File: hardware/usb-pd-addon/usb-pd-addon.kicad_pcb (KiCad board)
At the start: 4 copper layers, 48 x 40 mm, 61 parts, among them J1 Conn_02x10_Odd_Even, J10 Conn_01x03_Male, J11 Conn_01x03_Male, J12 Conn_01x03_Male, J2 Conn_02x10_Odd_Even, J3 USB_TYPE_C, J4 USB_TYPE_C, J5 Conn_01x03_Male, J6 TPAS, J7 TPBS, J8 Conn_02x03_Odd_Even, U1 FUSB302B, U2 AP2171W, U3 SN74AVC1T45DBVR, U4 SN74AVC1T45DBVR, U5 SN74AVC1T45DBVR, U6 SN74AVC1T45DBVR, U7 AP2127K-ADJ

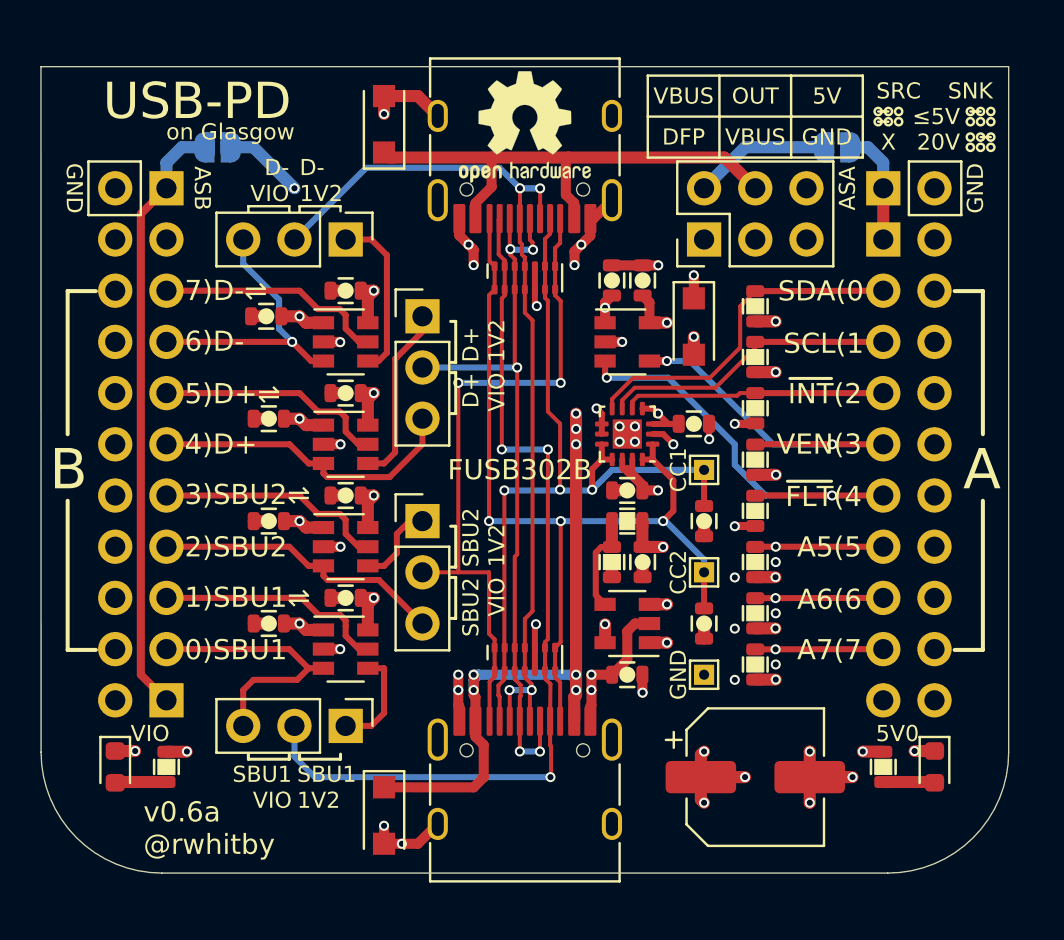
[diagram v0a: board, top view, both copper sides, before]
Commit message: v0.7a: analog switches instead of jumpers
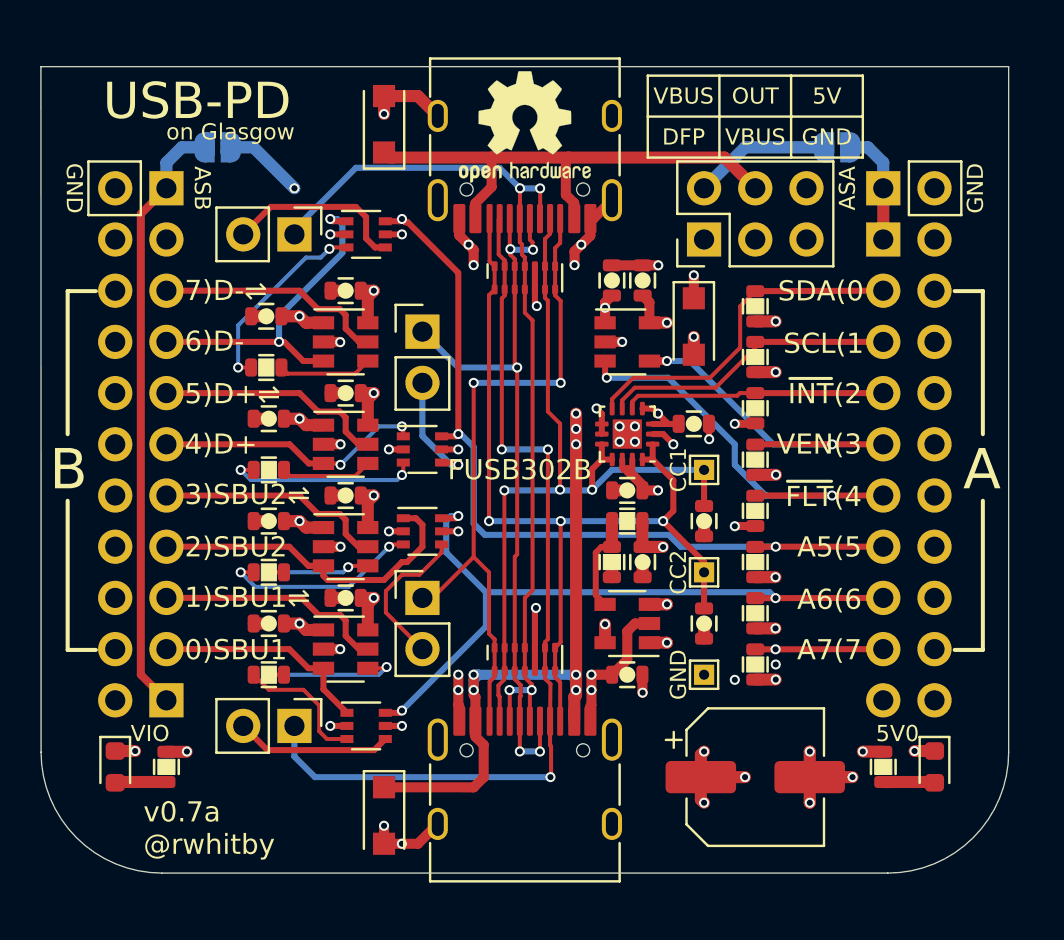
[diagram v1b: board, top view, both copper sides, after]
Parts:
- removed J12: Conn_01x03_Male, Connector_PinHeader_2.54mm:PinHeader_1x03_P2.54mm_Vertical
- added J9: Conn_01x02, Connector_PinHeader_2.54mm:PinHeader_1x02_P2.54mm_Vertical, F.Cu at (50.8, 45.2)
- added R11: 100R, pkl_dipol:R_0603, F.Cu at (43.1, 47.0)
- added R12: 100R, pkl_dipol:R_0603, F.Cu at (43.2, 57.1)
- added R13: 100R, pkl_dipol:R_0603, F.Cu at (43.2, 52.1)
- added R14: 100R, pkl_dipol:R_0603, F.Cu at (43.2, 62.2)
- added U10: NC7SB3157P6X, Package_TO_SOT_SMD:SOT-363_SC-70-6, F.Cu at (50.8, 55.1)
- added U11: NC7SB3157P6X, Package_TO_SOT_SMD:SOT-363_SC-70-6, F.Cu at (48.0, 64.8)
- added U8: NC7SB3157P6X, Package_TO_SOT_SMD:SOT-363_SC-70-6, F.Cu at (48.0, 40.4)
- added U9: NC7SB3157P6X, Package_TO_SOT_SMD:SOT-363_SC-70-6, F.Cu at (50.8, 51.1)
- J10, J11, J5: value Conn_01x03_Male -> Conn_01x02; footprint Connector_PinHeader_2.54mm:PinHeader_1x03_P2.54mm_Vertical -> Connector_PinHeader_2.54mm:PinHeader_1x02_P2.54mm_Vertical
- R6, R7: value 2K2 -> 1K
- moved J11 21.3 mm to (44.5, 64.8), turned to 270 degrees
- moved J10 3.81 mm to (50.8, 58.4)
- moved J5 2.55 mm to (44.5, 40.4)
- renumbered R11 to R10, R13 to R15, R33 to R16
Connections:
- net /A5 renamed /~USB_1V2
- net /A6 renamed /~SBU_1V2
- J10 pad 1: /SBU2_1V2 -> /SBU2
- J10 pad 2: /SBU2 -> Net-(J10-Pad2)
- J11 pad 1: /USBP_1V2 -> /SBU1
- J11 pad 2: /USBP -> Net-(J11-Pad2)
- J5 pad 1: /USBN_1V2 -> /USBN
- J5 pad 2: /USBN -> Net-(J5-Pad2)
- R6 pad 1: Net-(R6-Pad1) -> GND
- R7 pad 1: Net-(R7-Pad1) -> GND
- U3 pad 4: /USBN_1V2 -> Net-(R11-Pad1)
- U4 pad 4: /SBU2_1V2 -> Net-(R12-Pad1)
- U5 pad 4: /USBP_1V2 -> Net-(R13-Pad1)
- U6 pad 4: /SBU1_1V2 -> Net-(R14-Pad1)
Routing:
- net +5V: track 114.4 -> 162.9 mm, vias 14 -> 16
- net /~USB_1V2: track 6.35 -> 40.3 mm, vias 1 -> 3
- net /~SBU_1V2: track 6.35 -> 35.2 mm, vias 1 -> 3
- net Net-(R12-Pad2): track 0.00 -> 9.88 mm, vias 0 -> 2
- net Net-(R11-Pad2): track 0.00 -> 9.73 mm, vias 0 -> 2
- net Net-(R13-Pad2): track 0.00 -> 9.61 mm, vias 0 -> 2
- net Net-(J5-Pad2): track 0.00 -> 9.06 mm
- net /USBP_1V2: track 8.89 -> 0.00 mm
- net /USBN_1V2: track 8.33 -> 0.00 mm
- net Net-(J11-Pad2): track 0.00 -> 7.77 mm
- net Net-(J10-Pad2): track 0.00 -> 7.59 mm
- net Net-(R14-Pad1): track 0.00 -> 7.45 mm, vias 0 -> 2
- net Net-(R14-Pad2): track 0.00 -> 6.69 mm
- net GND: track 201.6 -> 207.5 mm, vias 48 -> 52
- net Net-(J9-Pad2): track 0.00 -> 5.88 mm, vias 0 -> 1
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- removed copper zone on In2.Cu, net +3V3
- removed copper zone on In2.Cu, net +5V
- removed copper zone on In2.Cu, net /1.2V
- removed copper zone on In2.Cu, net /VBUS
- removed copper zone on In2.Cu, net /VBUS_DFP
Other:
- board text added: "v0.7a @rwhitby"
- board text added: "v0.7a CC-BY-SA"
- board text removed: "20V"
- board text removed: "D+ 1V2"
- board text removed: "D+ VIO"
- board text removed: "D- 1V2"
- board text removed: "D- VIO"
- board text removed: "SBU1 1V2"
- board text removed: "SBU1 VIO"
- board text removed: "SBU2 1V2"
- board text removed: "SBU2 VIO"
- board text removed: "SNK"
- board text removed: "SRC"
- board text removed: "X"
- board text removed: "v0.6a @rwhitby"
- board text removed: "v0.6a CC-BY-SA"
- board text removed: "≤5V"

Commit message: Interim version for review
Changed level shifters to smaller footprint.
Added pull-down resistors on direction signals and analog switch selects.
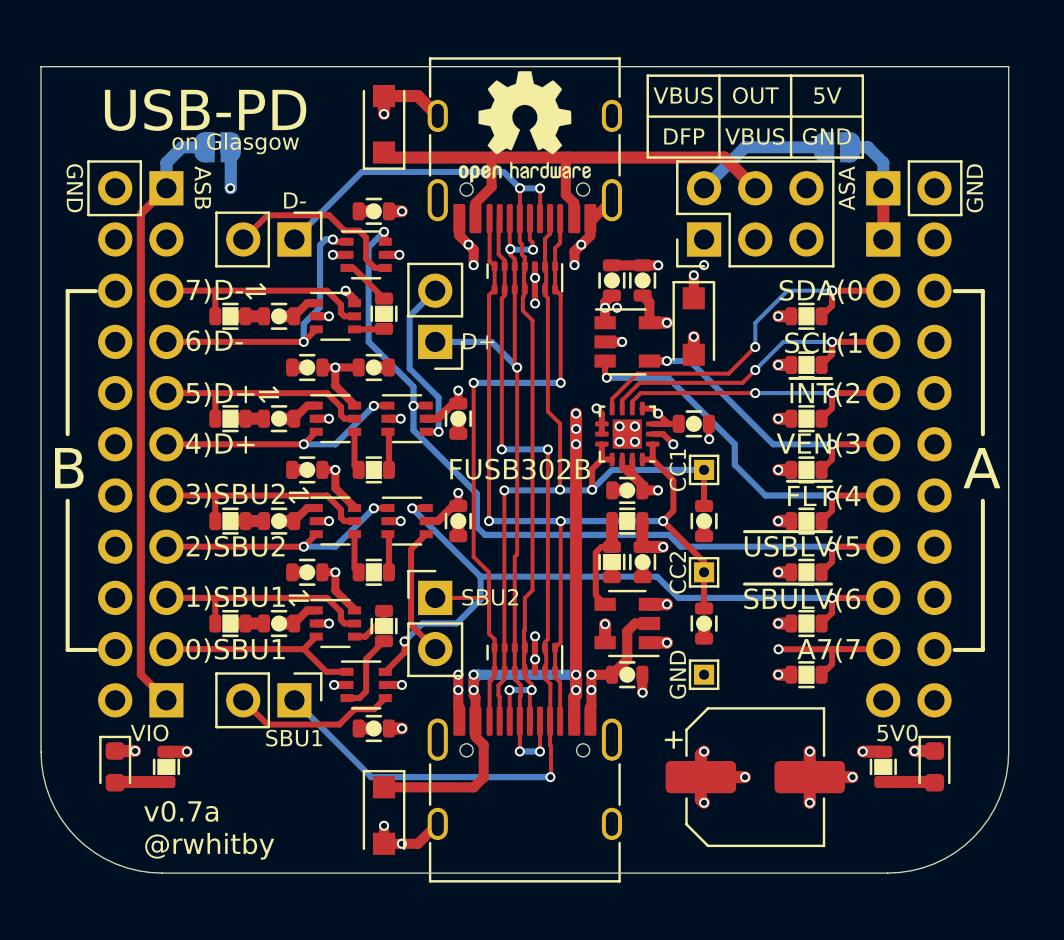
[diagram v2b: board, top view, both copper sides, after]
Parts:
- added C18: 0.1u, pkl_dipol:C_0603, F.Cu at (48.4, 39.2)
- added C19: 0.1u, pkl_dipol:C_0603, F.Cu at (52.6, 49.5)
- added C20: 0.1u, pkl_dipol:C_0603, F.Cu at (52.6, 54.6)
- added C21: 0.1u, pkl_dipol:C_0603, F.Cu at (48.4, 64.9)
- added R17: 100K, pkl_dipol:R_0603, F.Cu at (41.3, 44.5)
- added R18: 100K, pkl_dipol:R_0603, F.Cu at (41.3, 54.6)
- added R19: 100K, pkl_dipol:R_0603, F.Cu at (41.3, 49.5)
- added R20: 100K, pkl_dipol:R_0603, F.Cu at (41.3, 59.7)
- R6, R7: value 1K -> 100K
- U3, U4, U5: value SN74AVC1T45DBVR -> SN74AVC1T45DCKR; footprint Package_TO_SOT_SMD:SOT-23-6 -> Package_TO_SOT_SMD:SOT-363_SC-70-6
- U6: footprint Package_TO_SOT_SMD:SOT-23-6 -> Package_TO_SOT_SMD:SOT-363_SC-70-6
- moved R11 6.42 mm to (48.9, 44.3), turned to 90 degrees
- moved R14 6.20 mm to (48.9, 59.8), turned to 270 degrees
- moved R12 5.21 mm to (48.4, 57.1), turned to 0 degrees
- moved R13 5.21 mm to (48.4, 52.1), turned to 0 degrees
- moved C3 4.06 mm to (48.4, 47.0), turned to 0 degrees
- moved R3 2.59 mm to (69.8, 49.5), turned to 0 degrees
- moved R4 2.59 mm to (69.8, 52.1), turned to 0 degrees
- moved R5 2.59 mm to (69.8, 54.6), turned to 180 degrees
- moved R6 2.59 mm to (69.8, 57.1), turned to 0 degrees
- moved R7 2.59 mm to (69.8, 59.7), turned to 0 degrees
- moved R8 2.59 mm to (69.8, 62.2), turned to 0 degrees
- moved R1 2.59 mm to (69.8, 44.5), turned to 0 degrees
- moved R2 2.57 mm to (69.8, 46.9), turned to 0 degrees
- moved C12 2.29 mm to (45.1, 57.1)
- moved C4 2.29 mm to (45.1, 52.1)
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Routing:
- net +5V: track 162.9 -> 171.5 mm, vias 16 -> 17
- net Net-(R12-Pad2): track 9.88 -> 1.91 mm, vias 2 -> 0
- net Net-(R13-Pad2): track 9.61 -> 1.91 mm, vias 2 -> 0
- net Net-(R11-Pad2): track 9.73 -> 2.47 mm, vias 2 -> 0
- net Net-(R14-Pad1): track 7.45 -> 2.19 mm, vias 2 -> 0
- net /SBU2_3V3: track 16.5 -> 12.7 mm, vias 0 -> 2
- net Net-(R12-Pad1): track 5.54 -> 1.97 mm, vias 2 -> 0
- net Net-(R11-Pad1): track 4.67 -> 1.47 mm
- net Net-(J9-Pad2): track 5.88 -> 8.99 mm
- net /1.2V: track 58.3 -> 61.1 mm
- net Net-(R14-Pad2): track 6.69 -> 3.95 mm
- net Net-(R13-Pad1): track 4.61 -> 1.97 mm
- net /USBN_3V3: track 16.9 -> 14.3 mm
- net /~FLT: track 21.4 -> 19.1 mm
- net /VEN: track 17.1 -> 14.8 mm
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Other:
- board text added: "5)~USBLV"
- board text added: "6)~SBULV"
- board text added: "D+"
- board text added: "D-"
- board text added: "SBU1"
- board text added: "SBU2"
- board text added: "~SBULV~(6"
- board text added: "~USBLV~(5"
- board text removed: "5)A5"
- board text removed: "6)A6"
- board text removed: "A5(5"
- board text removed: "A6(6"

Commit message: Widened some power traces.
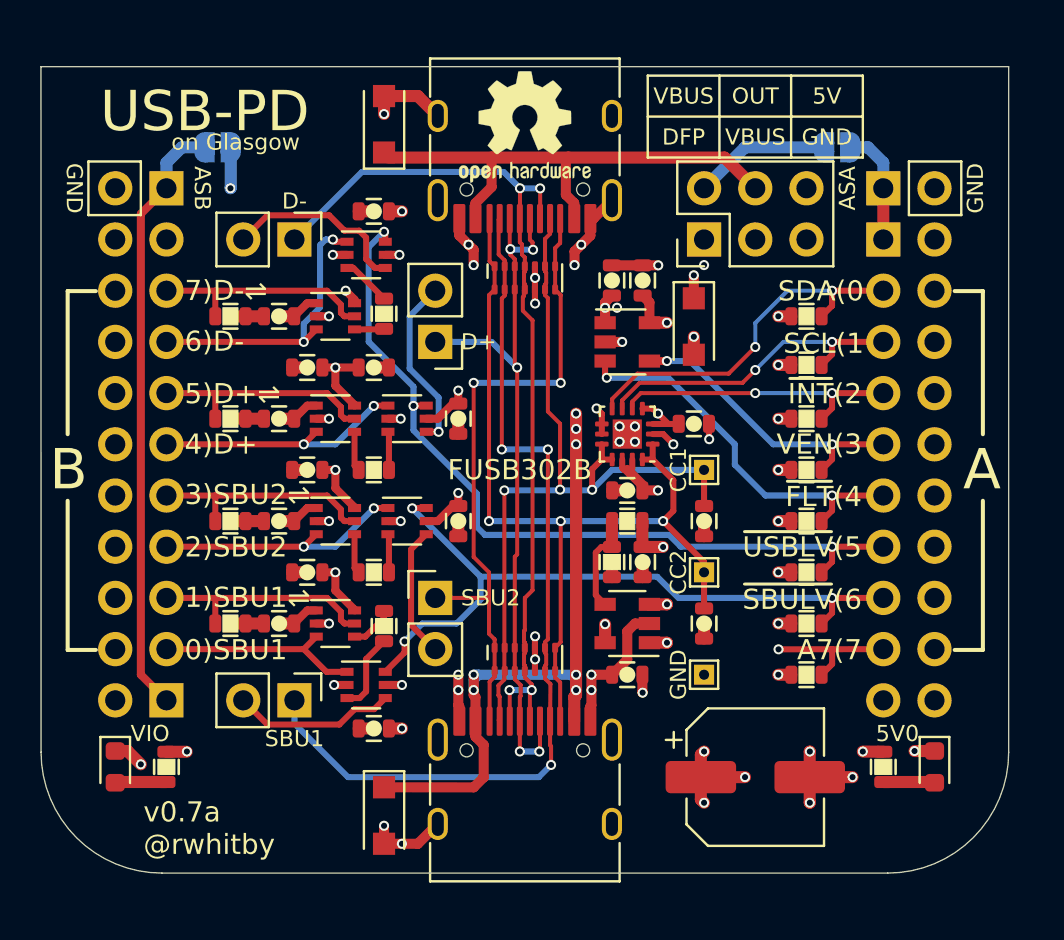
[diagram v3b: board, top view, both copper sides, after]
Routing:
- net +5V: track 171.5 -> 172.5 mm
- net GND: track 209.6 -> 210.2 mm
- net /SDA: vias 3 -> 2

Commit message: v0.8a: Colocated D+/D- and SBU1/SBU2 jumpers. Moved ASA/ASB jumpers away from Glasgow headers.
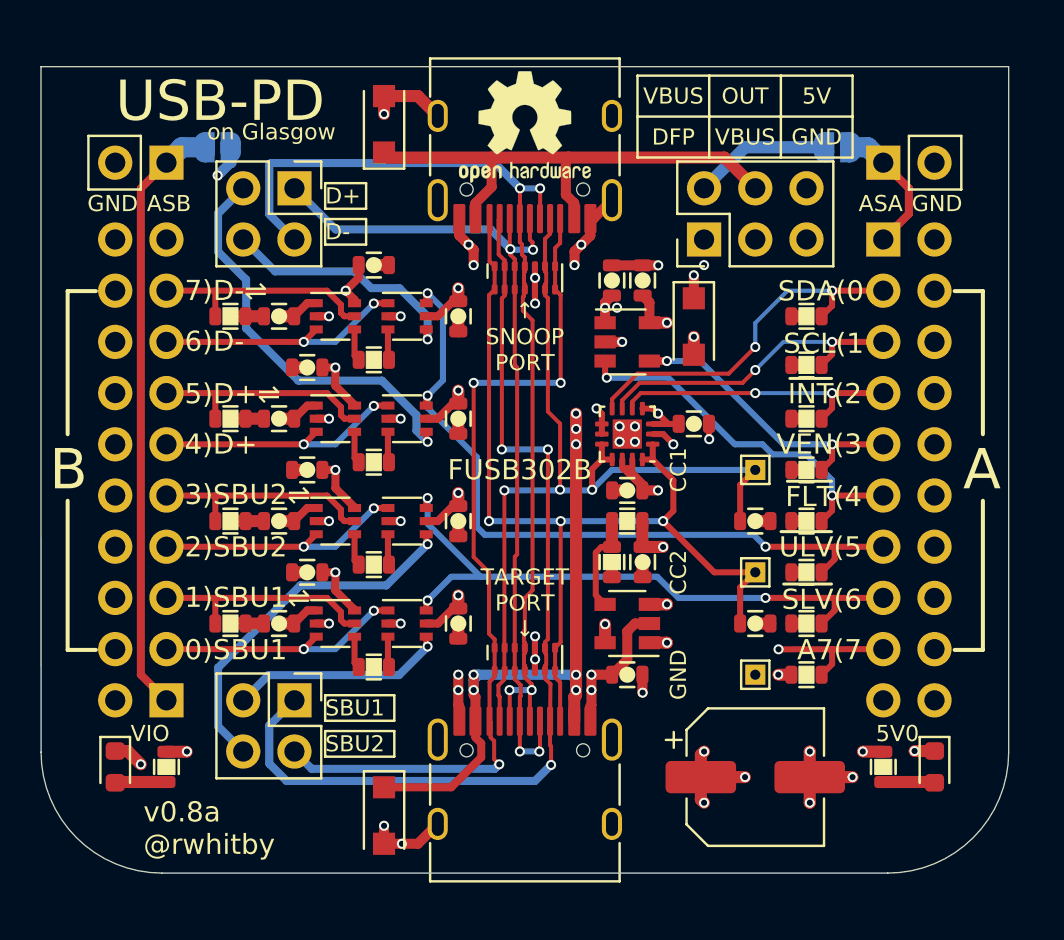
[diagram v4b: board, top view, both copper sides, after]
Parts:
- removed J10, J5: Conn_01x02, Connector_PinHeader_2.54mm:PinHeader_1x02_P2.54mm_Vertical
- J11, J9: value Conn_01x02 -> Conn_02x02; footprint Connector_PinHeader_2.54mm:PinHeader_1x02_P2.54mm_Vertical -> Connector_PinHeader_2.54mm:PinHeader_2x02_P2.54mm_Vertical
- moved J9 10.3 mm to (44.5, 38.1), turned to 270 degrees
- moved C21 6.68 mm to (52.6, 59.7), turned to 270 degrees
- moved C18 6.68 mm to (52.6, 44.5), turned to 270 degrees
- moved C3 5.08 mm to (48.4, 41.9)
- moved U11 3.66 mm to (50.0, 59.7)
- moved U8 3.66 mm to (50.0, 44.5)
- moved C15 2.54 mm to (67.3, 54.6), turned to 180 degrees
- moved C17 2.54 mm to (67.3, 59.7), turned to 180 degrees
- moved TP1 2.54 mm to (67.3, 52.1)
- moved TP2 2.54 mm to (67.3, 57.1)
- moved TP3 2.54 mm to (67.3, 62.2)
- moved R11 2.34 mm to (48.4, 46.6), turned to 0 degrees
- moved R14 2.09 mm to (48.4, 61.8), turned to 0 degrees
- moved J6 1.27 mm to (73.7, 36.8)
- moved J7 1.27 mm to (38.1, 36.8)
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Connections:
- J11 pad 2: Net-(J11-Pad2) -> /SBU2
- J9 pad 2: Net-(J9-Pad2) -> /USBN
- U10 pad 4: Net-(J10-Pad2) -> Net-(J11-Pad4)
- U11 pad 4: Net-(J11-Pad2) -> Net-(J11-Pad3)
- U8 pad 4: Net-(J5-Pad2) -> Net-(J9-Pad4)
- U9 pad 4: Net-(J9-Pad2) -> Net-(J9-Pad3)
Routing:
- net Net-(J9-Pad3): track 0.00 -> 20.3 mm, vias 0 -> 1
- net Net-(J11-Pad4): track 0.00 -> 18.1 mm, vias 0 -> 1
- net Net-(J9-Pad4): track 0.00 -> 12.4 mm, vias 0 -> 1
- net +5V: track 172.5 -> 160.6 mm, vias 17 -> 15
- net Net-(J11-Pad3): track 0.00 -> 10.8 mm, vias 0 -> 1
- net /SBU2: track 32.8 -> 43.1 mm, vias 2 -> 3
- net Net-(J5-Pad2): track 9.25 -> 0.00 mm
- net Net-(J9-Pad2): track 8.99 -> 0.00 mm, vias 1 -> 0
- net Net-(J11-Pad2): track 8.09 -> 0.00 mm
- net /USBP: track 37.1 -> 44.3 mm, vias 5 -> 4
- net Net-(J10-Pad2): track 6.51 -> 0.00 mm
- net /USBN: track 45.3 -> 49.6 mm
- net /~USB_1V2: track 40.4 -> 36.4 mm
- net /~SBU_1V2: track 35.1 -> 31.1 mm
- net /CC1: track 40.7 -> 44.3 mm
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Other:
- board text added: "5)~ULV"
- board text added: "6)~SLV"
- board text added: "TARGET PORT ↓"
- board text added: "v0.8a @rwhitby"
- board text added: "v0.8a CC-BY-SA"
- board text added: "~SLV~(6"
- board text added: "~ULV~(5"
- board text added: "↑ SNOOP PORT"
- board text removed: "5)~USBLV"
- board text removed: "6)~SBULV"
- board text removed: "v0.7a @rwhitby"
- board text removed: "v0.7a CC-BY-SA"
- board text removed: "~SBULV~(6"
- board text removed: "~USBLV~(5"
